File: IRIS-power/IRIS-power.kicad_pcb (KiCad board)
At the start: 2 copper layers, 66.9 x 65 mm, 82 parts, among them J101 Powerpole, J102 PJ-047AH, J801 IRIS_physical, Q21 2N7002, Q601 IRLML6402, U101 TVS1400DRV, U102 TVS1400DRV, U21 MAX17261, U31 TPS2121, U41 TPS55340, U51 TPSM53604, U601 LTC3110, U602 PCA9537, U701 TLV75733PDBV

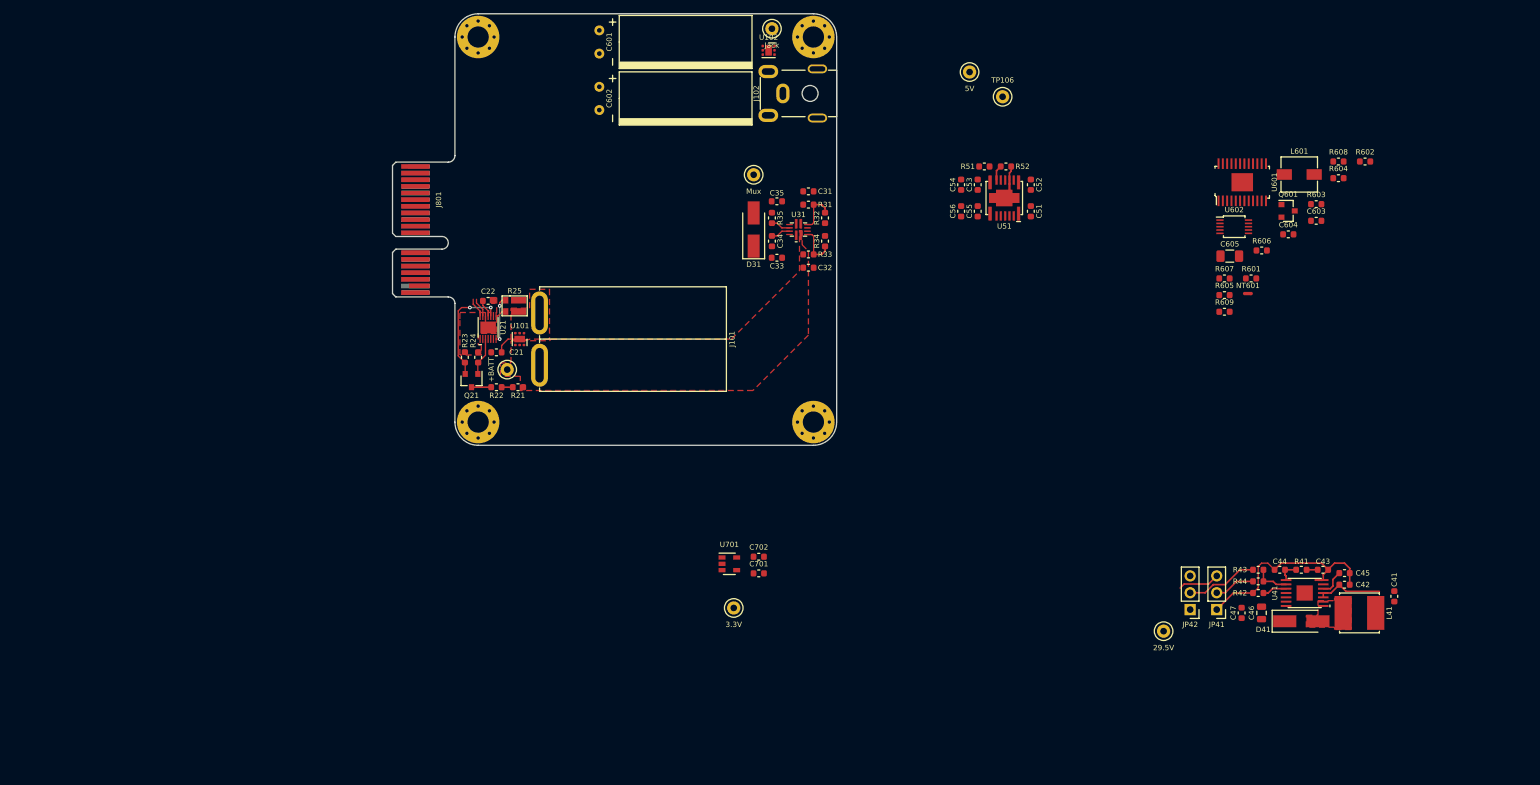
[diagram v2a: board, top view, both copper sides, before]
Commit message: Updated layout
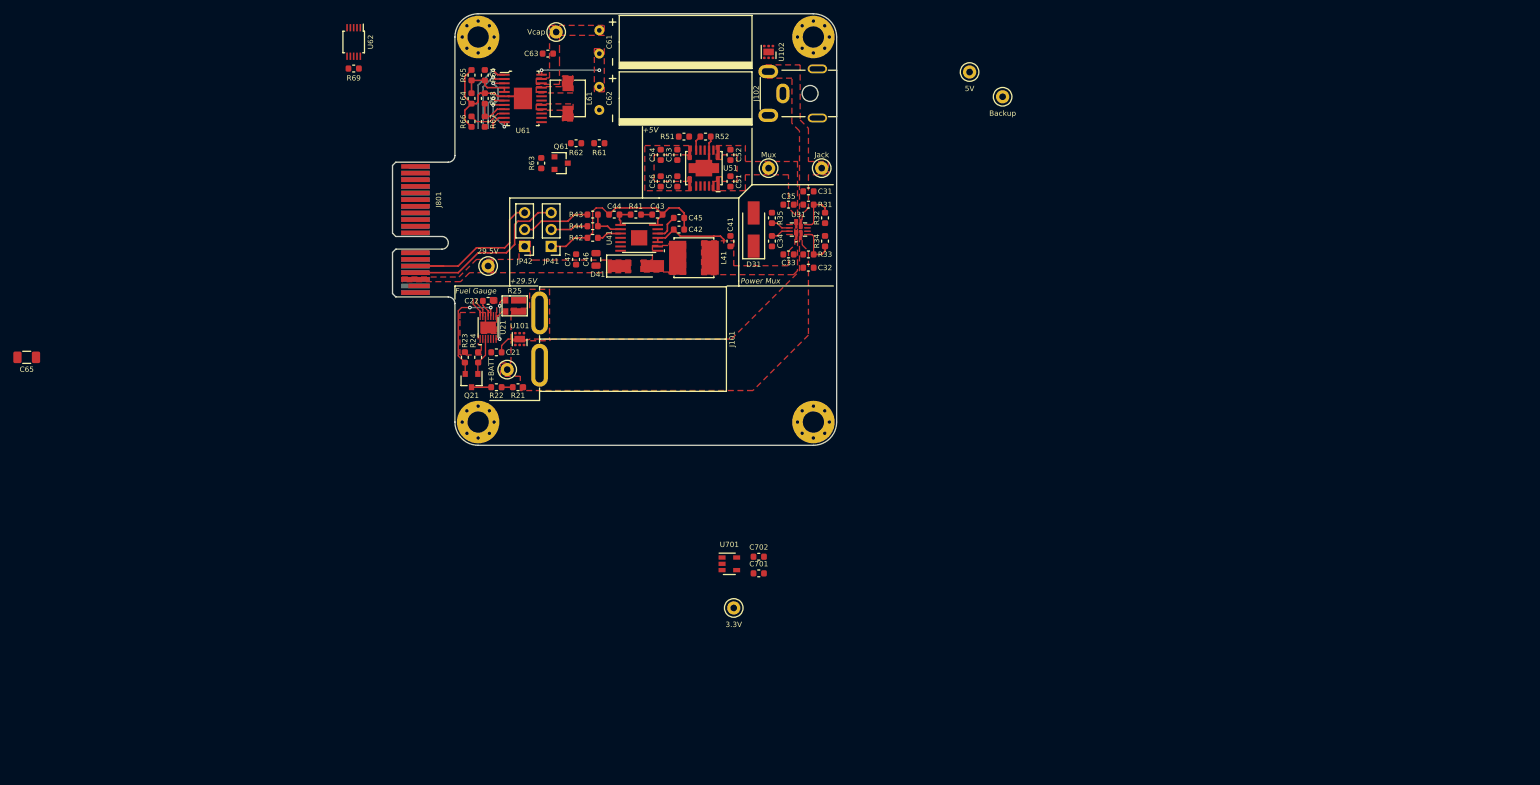
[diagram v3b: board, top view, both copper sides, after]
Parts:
- removed R606: 3k, Resistor_SMD:R_0603_1608Metric
- added R66: 3k, Resistor_SMD:R_0603_1608Metric, F.Cu at (2.50, 16.2)
- added TP61: Vcap, TestPoint:TestPoint_Keystone_5000-5004_Miniature, F.Cu at (15.2, 2.75)
- moved C65 181.9 mm to (-64.5, 51.8), turned to 180 degrees
- moved R69 136.2 mm to (-15.2, 8.25), turned to 180 degrees
- moved U62 135.5 mm to (-15.2, 4.25), turned to 270 degrees
- moved R64 129.5 mm to (4.50, 9.25), turned to 90 degrees
- moved R68 128.9 mm to (4.50, 12.8), turned to 90 degrees
- moved C64 124.7 mm to (2.50, 12.8), turned to 270 degrees
- moved R62 118.9 mm to (18.2, 19.5), turned to 180 degrees
- moved C63 118.4 mm to (14.0, 6.00), turned to 180 degrees
- moved R65 118.2 mm to (2.50, 9.25), turned to 270 degrees
- moved R63 116.9 mm to (13.0, 22.5), turned to 90 degrees
- moved TP105 115.7 mm to (5.00, 38.0)
- moved NT61 114.8 mm to (8.57, 12.4)
- moved JP41 114.2 mm to (14.5, 35.0)
- moved JP42 114.2 mm to (10.5, 35.0)
- moved R67 113.9 mm to (4.50, 16.2), turned to 90 degrees
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- renumbered C601 to C61, C602 to C62, C603 to C63, C604 to C64, C605 to C65, L601 to L61, NT601 to NT61, Q601 to Q61, R601 to R61, R602 to R62, R603 to R63, R604 to R64, R605 to R65, R607 to R67, R608 to R68, R609 to R69, U601 to U61, U602 to U62
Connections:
- net Net-(C604-Pad1) renamed /5V Backup/FBVcap
- net Net-(L601-Pad1) renamed /5V Backup/SW1
- net Net-(L601-Pad2) renamed /5V Backup/SW2
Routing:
- net /Edge Connector/FB_HV_P: track 0.00 -> 26.0 mm
- net /Edge Connector/FB_HV_N: track 6.26 -> 26.0 mm
- net GNDS: track 0.00 -> 16.7 mm
- net /3V Supply/VSYS: track 0.00 -> 11.9 mm, vias 0 -> 3
- net /5V Backup/CAP_OK: track 0.00 -> 11.7 mm, vias 0 -> 1
- net /5V Backup/~CMP_OUT: track 0.00 -> 10.2 mm, vias 0 -> 1
- net /5V Backup/Vmid: track 0.00 -> 9.38 mm, vias 0 -> 2
- net /5V Backup/FBVcap: track 0.00 -> 8.39 mm
- net /5V Backup/DIR: track 0.00 -> 6.65 mm, vias 0 -> 1
- net /5V Backup/PROG: track 0.00 -> 5.78 mm
- net /5V Backup/FB: track 0.00 -> 5.33 mm
- net /5V Backup/~CHRG: track 0.00 -> 2.79 mm
- net /5V Supply/+MUX: track 10.0 -> 12.2 mm
- net Net-(JP41-Pad2): track 6.17 -> 5.67 mm
- net Net-(JP42-Pad2): track 10.9 -> 10.4 mm
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- added copper zone on F.Cu, net /5V Backup/+5V
- added copper zone on F.Cu, net /5V Backup/SW1
- added copper zone on F.Cu, net /5V Backup/SW2
- added copper zone on F.Cu, net /5V Backup/Vcap
- added copper zone on F.Cu, net /5V Backup/Vmid
- added copper zone on F.Cu, net /5V Supply/+MUX
- added copper zone on F.Cu, net /Edge Connector/+29.5V
- added copper zone on F.Cu, net /Power Mux/VDC
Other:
- board text added: "+29.5V"
- board text added: "+5V"
- board text added: "Fuel Gauge"
- board text added: "Power Mux"

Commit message: Updated layout
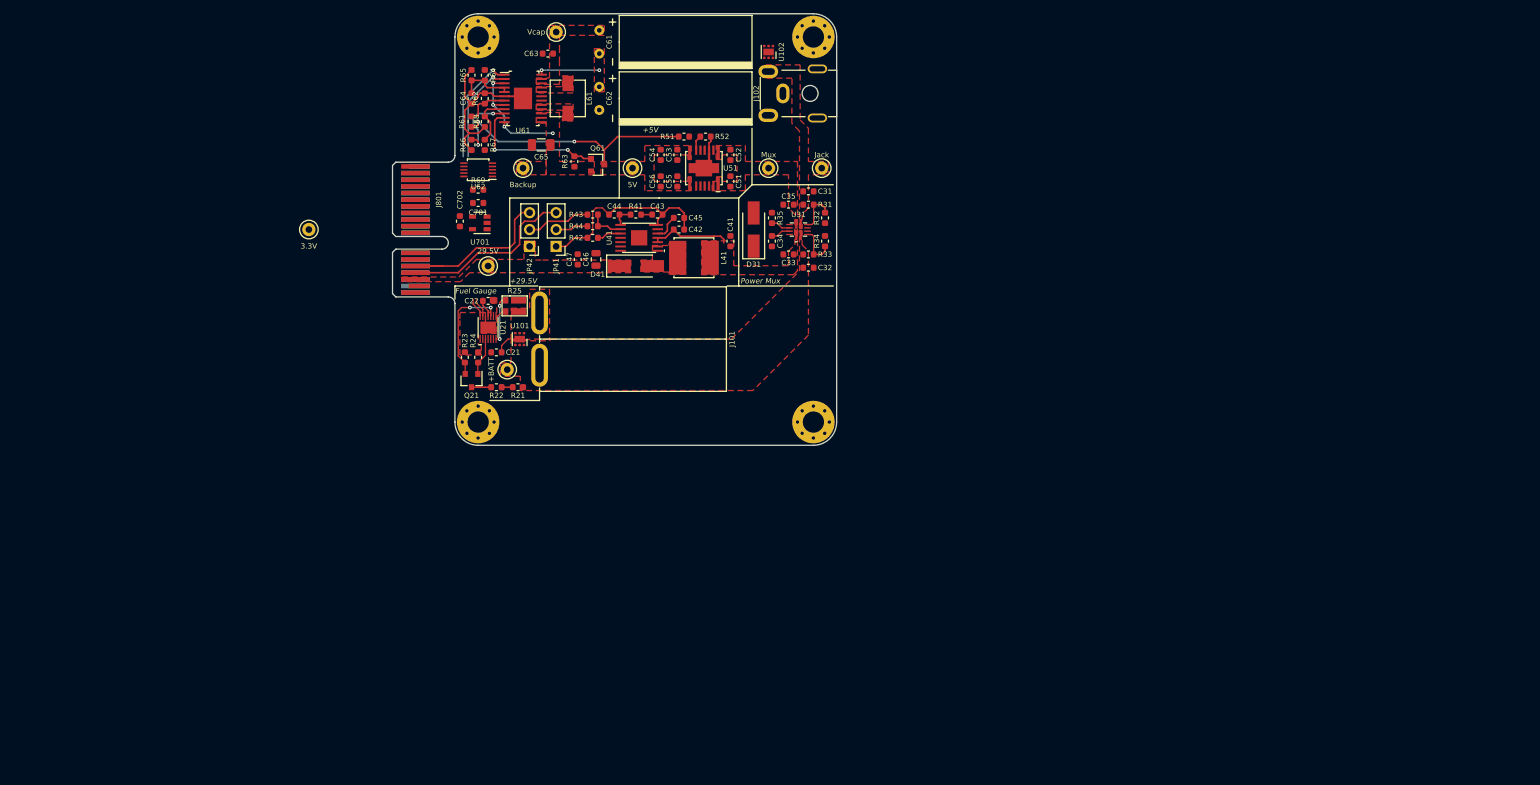
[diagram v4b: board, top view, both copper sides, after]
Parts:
- moved TP107 85.7 mm to (-22.0, 32.5)
- moved C65 83.8 mm to (13.0, 19.8)
- moved TP106 73.0 mm to (10.2, 23.2)
- moved C701 70.0 mm to (3.50, 28.5), turned to 180 degrees
- moved C702 67.7 mm to (0.75, 31.2), turned to 90 degrees
- moved U701 63.6 mm to (3.75, 31.5), turned to 180 degrees
- moved TP104 52.8 mm to (26.8, 23.2)
- moved U62 26.9 mm to (3.50, 23.5), turned to 180 degrees
- moved R69 26.2 mm to (3.50, 26.5), turned to 0 degrees
- moved R61 19.5 mm to (2.50, 16.2), turned to 90 degrees
- moved R62 15.3 mm to (4.50, 12.8), turned to 90 degrees
- moved Q61 5.51 mm to (21.5, 22.8)
- moved R63 5.01 mm to (18.0, 22.2)
- moved R66 3.50 mm to (2.50, 19.8)
- moved R67 3.50 mm to (4.50, 19.8)
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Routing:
- net /5V Backup/+5V: track 0.00 -> 36.7 mm, vias 0 -> 2
- net /5V Backup/~CHRG: track 2.79 -> 21.1 mm, vias 0 -> 2
- net /3V Supply/VSYS: track 11.9 -> 19.0 mm, vias 3 -> 4
- net GNDS: track 16.7 -> 23.0 mm
- net /5V Backup/~CMP_OUT: track 10.2 -> 15.4 mm
- net /5V Backup/CAP_OK: track 11.7 -> 16.8 mm
- net /5V Backup/PROG: track 5.78 -> 10.9 mm, vias 0 -> 2
- net /5V Backup/FB: track 5.33 -> 8.02 mm
- net Net-(JP41-Pad2): track 5.67 -> 4.92 mm
- net /HV Supply/AGND: track 30.6 -> 29.9 mm
- net /Edge Connector/FB_HV_P: track 26.0 -> 26.8 mm
- net Net-(JP42-Pad2): track 10.4 -> 10.9 mm
- net /5V Backup/DIR: track 6.65 -> 6.82 mm, vias 1 -> 0
- added copper zone on F.Cu, net /3V Supply/VSYS

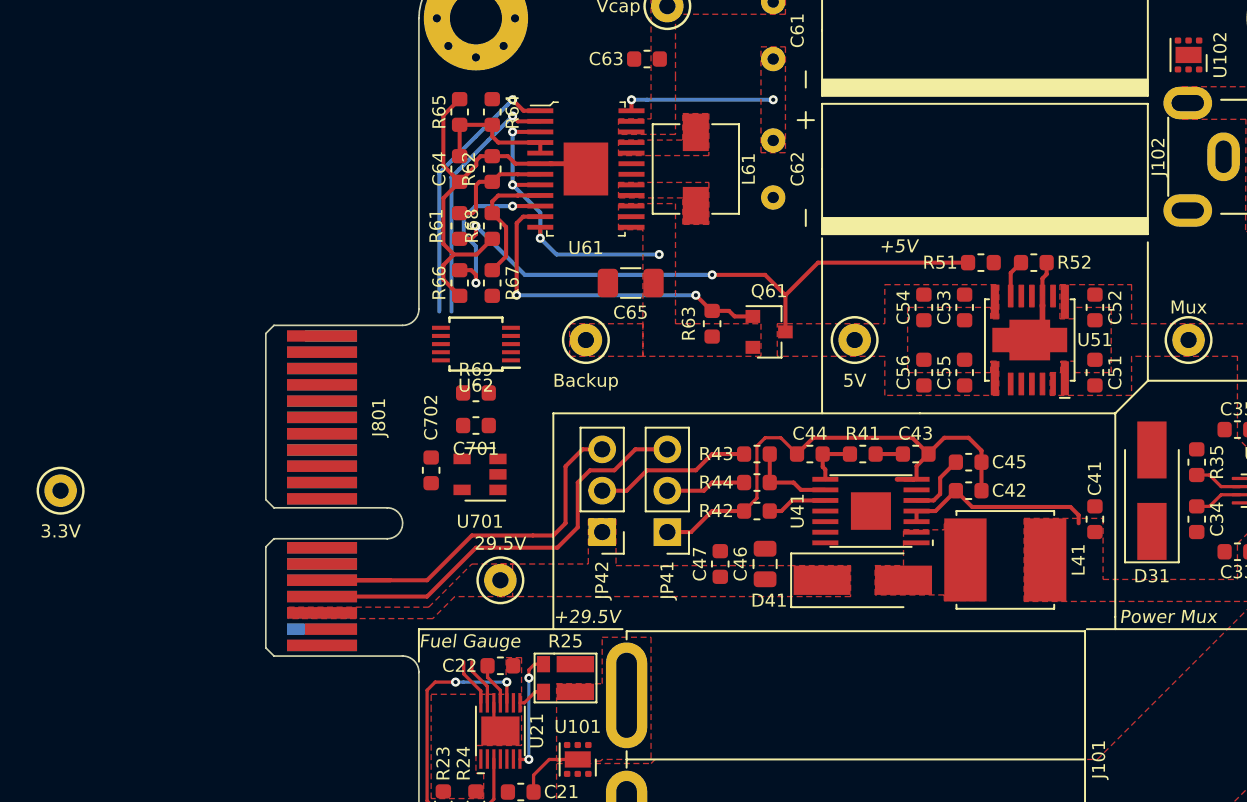
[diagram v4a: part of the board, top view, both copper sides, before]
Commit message: Finished initial layout without gnd plane
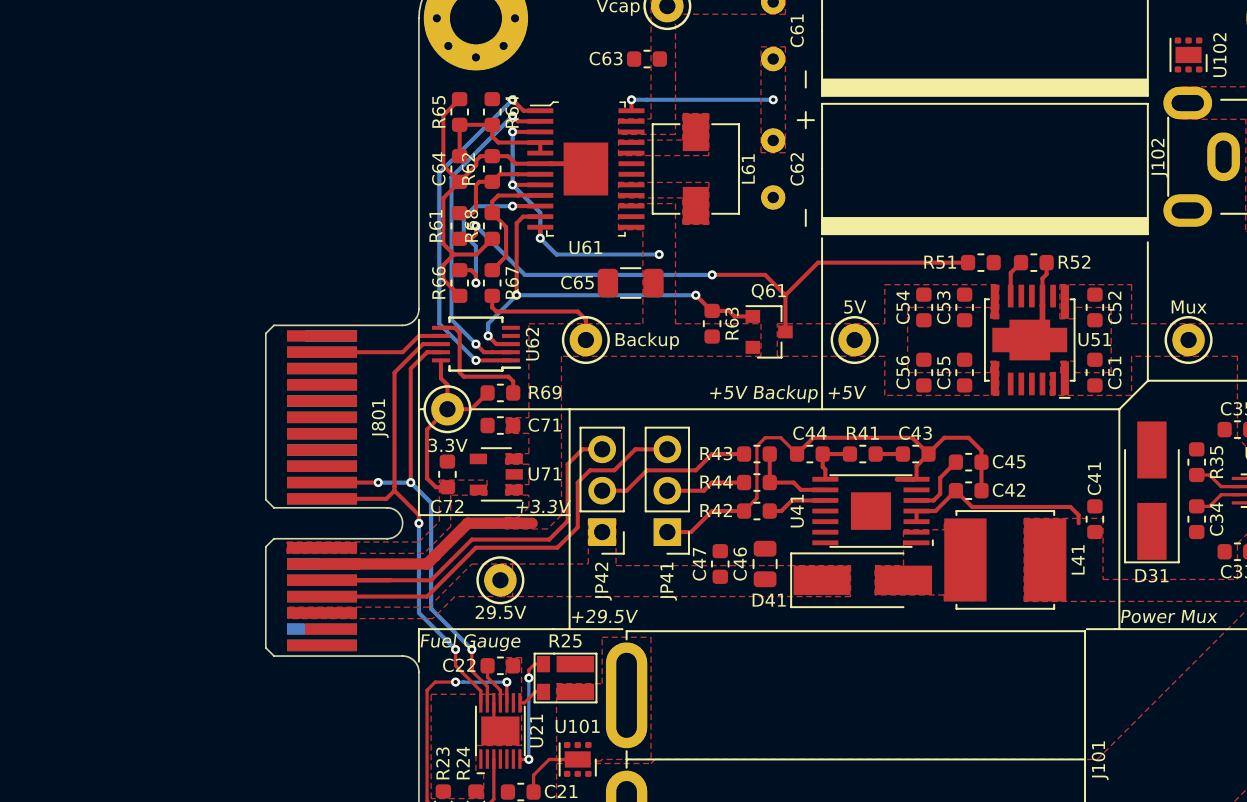
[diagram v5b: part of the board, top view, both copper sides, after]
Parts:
- removed C701: 1uF, Capacitor_SMD:C_0603_1608Metric
- added C71: 1uF, Capacitor_SMD:C_0603_1608Metric, F.Cu at (5.00, 28.5)
- moved TP107 24.3 mm to (1.75, 27.5)
- moved R69 1.50 mm to (5.00, 26.5)
- moved C72 1.03 mm to (1.75, 31.5)
- moved U71 1.00 mm to (4.75, 31.5)
- renumbered C702 to C72, U701 to U71
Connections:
- U62 pad 1: /5V Backup/~CHRG -> /5V Backup/CAP_OK
- U62 pad 2: /5V Backup/CAP_OK -> /5V Backup/~CMP_OUT
- U62 pad 3: /5V Backup/~CMP_OUT -> /5V Backup/~CHRG
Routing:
- net /5V Backup/SDA: track 2.92 -> 30.8 mm, vias 0 -> 3
- net /5V Backup/SCL: track 2.96 -> 30.7 mm, vias 0 -> 2
- net /3V Supply/VSYS: track 19.0 -> 41.0 mm
- net /3V Supply/+3.3V: track 0.00 -> 12.3 mm
- net Net-(R69-Pad2): track 0.00 -> 7.95 mm
- net /5V Backup/~INT: track 0.00 -> 7.71 mm
- net /5V Backup/CAP_OK: track 16.8 -> 22.9 mm, vias 1 -> 2
- net /5V Backup/~CMP_OUT: track 15.4 -> 20.4 mm, vias 1 -> 2
- net /5V Backup/~CHRG: track 21.1 -> 25.9 mm, vias 2 -> 3
- net Net-(JP42-Pad2): track 10.9 -> 9.64 mm
- added copper zone on F.Cu, net /3V Supply/+3.3V
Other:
- board text added: "+3.3V"
- board text added: "+5V Backup"
